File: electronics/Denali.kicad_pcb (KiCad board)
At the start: 2 copper layers, 91 parts, among them SW1 SW_SPST, SW10 SW_SPST, SW11 SW_SPST, SW12 SW_SPST, SW13 SW_SPST, SW14 SW_SPST, SW15 SW_SPST, SW16 SW_SPST, SW17 SW_SPST, SW18 SW_SPST, SW19 SW_SPST, SW2 SW_SPST, SW20 SW_SPST, SW21 SW_SPST, SW22 SW_SPST, SW23 SW_SPST, SW24 SW_SPST, SW25 SW_SPST, SW26 SW_SPST, SW27 SW_SPST, SW28 SW_SPST, SW29 SW_SPST, SW3 SW_SPST, SW30 SW_SPST, SW31 SW_SPST, SW32 SW_SPST, SW33 SW_SPST, SW34 SW_SPST, SW35 SW_SPST, SW36 SW_SPST, SW37 SW_SPST, SW38 SW_SPST, SW39 SW_SPST, SW4 SW_SPST, SW40 SW_SPST, SW41 SW_SPST, SW42 SW_SPST, SW43 SW_SPST, SW44 SW_SPST, SW45 SW_SPST, SW46 SW_SPST, SW47 SW_SPST, SW48 SW_SPST, SW49 SW_SPST, SW5 SW_SPST, SW50 SW_SPST, SW51 SW_SPST, SW52 SW_SPST, SW53 SW_SPST, SW54 SW_SPST, SW55 SW_SPST, SW56 SW_SPST, SW57 SW_SPST, SW58 SW_SPST, SW59 SW_SPST, SW6 SW_SPST, SW60 SW_SPST, SW61 SW_SPST, SW62 SW_SPST, SW63 SW_SPST, SW64 SW_SPST, SW65 SW_SPST, SW66 SW_SPST, SW67 SW_SPST, SW68 SW_SPST, SW69 SW_SPST, SW7 SW_SPST, SW70 SW_SPST, SW71 SW_SPST, SW72 SW_SPST, SW73 SW_SPST, SW74 SW_SPST, SW75 SW_SPST, SW76 SW_SPST, SW77 SW_SPST, SW78 SW_SPST, SW79 SW_SPST, SW8 SW_SPST, SW80 SW_SPST, SW81 SW_SPST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

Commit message: layout components
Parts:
- removed the SW1 at (57.0, 134.0)
- removed SW10, SW11, SW12, SW13, SW15, SW16, SW17, SW18, SW19, SW7, SW78, SW79, SW8, SW80, SW81, SW83, SW9: SW_SPST, Kailh:Kailh_socket_MX
- added SW100: SW_SPST, Kailh:Kailh_socket_MX, F.Cu at (452.0, 215.7)
- added SW101: SW_SPST, Kailh:Kailh_socket_MX, F.Cu at (471.0, 215.7)
- added SW102: SW_SPST, Kailh:Kailh_socket_MX, F.Cu at (490.0, 225.0)
- added SW104: SW_SPST, Kailh:Kailh_socket_MX, F.Cu at (442.0, 234.0)
- added SW105: SW_SPST, Kailh:Kailh_socket_MX, F.Cu at (471.0, 234.7)
- added SW87: SW_SPST, Kailh:Kailh_socket_MX, F.Cu at (413.0, 234.7)
- added SW88: SW_SPST, Kailh:Kailh_socket_MX, F.Cu at (452.0, 158.7)
- added SW89: SW_SPST, Kailh:Kailh_socket_MX, F.Cu at (471.0, 158.7)
- added SW90: SW_SPST, Kailh:Kailh_socket_MX, F.Cu at (490.0, 158.7)
- added SW91: SW_SPST, Kailh:Kailh_socket_MX, F.Cu at (433.0, 177.7)
- added SW92: SW_SPST, Kailh:Kailh_socket_MX, F.Cu at (452.0, 177.7)
- added SW93: SW_SPST, Kailh:Kailh_socket_MX, F.Cu at (471.0, 177.7)
- added SW94: SW_SPST, Kailh:Kailh_socket_MX, F.Cu at (490.0, 188.0)
- added SW95: SW_SPST, Kailh:Kailh_socket_MX, F.Cu at (433.0, 196.7)
- added SW96: SW_SPST, Kailh:Kailh_socket_MX, F.Cu at (452.0, 196.7)
- added SW97: SW_SPST, Kailh:Kailh_socket_MX, F.Cu at (471.0, 196.7)
- added SW99: SW_SPST, Kailh:Kailh_socket_MX, F.Cu at (433.0, 215.7)
- moved SW48 321.6 mm to (355.0, 158.7)
- moved SW47 306.3 mm to (336.0, 158.7)
- moved SW58 292.8 mm to (317.0, 196.7)
- moved SW51 276.2 mm to (298.0, 177.7)
- moved SW84 274.7 mm to (433.0, 158.7)
- moved SW86 264.1 mm to (394.0, 234.7)
- moved SW57 260.8 mm to (298.0, 196.7)
- moved SW82 254.6 mm to (394.0, 215.7)
- moved SW40 254.2 mm to (260.0, 158.7)
- moved SW42 247.2 mm to (202.0, 234.7)
- moved SW54 246.4 mm to (355.0, 177.7)
- moved SW53 246.0 mm to (336.0, 177.7)
- moved SW85 241.3 mm to (375.0, 234.7)
- moved SW73 240.8 mm to (355.0, 234.7)
- moved SW76 237.1 mm to (394.0, 177.7)
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- renumbered SW14 to SW1
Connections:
- SW2 pad 1: SW2 -> SW14
- SW20 pad 1: SW20 -> SW14
- SW21 pad 1: SW21 -> SW14
- SW22 pad 1: SW22 -> SW14
- SW23 pad 1: SW23 -> SW14
- SW24 pad 1: SW24 -> SW14
- SW25 pad 1: SW25 -> SW14
- SW26 pad 1: SW26 -> SW14
- SW27 pad 1: SW27 -> SW14
- SW28 pad 1: SW28 -> SW14
- SW29 pad 1: SW29 -> SW14
- SW3 pad 1: SW3 -> SW14
- SW30 pad 1: SW30 -> SW14
- SW31 pad 1: SW31 -> SW14
- SW32 pad 1: SW32 -> SW14
- SW33 pad 1: SW33 -> SW14
- SW34 pad 1: SW34 -> SW14
- SW35 pad 1: SW35 -> SW14
- SW36 pad 1: SW36 -> SW14
- SW37 pad 1: SW37 -> SW14
- SW38 pad 1: SW38 -> SW14
- SW39 pad 1: SW39 -> SW14
- SW4 pad 1: SW4 -> SW14
- SW41 pad 1: SW41 -> SW14
- SW42 pad 1: SW42 -> SW14
- SW43 pad 1: SW43 -> SW40
- SW44 pad 1: SW44 -> SW14
- SW45 pad 1: SW45 -> SW40
- SW46 pad 1: SW46 -> SW40
- SW47 pad 1: SW47 -> SW40
- SW48 pad 1: SW48 -> SW40
- SW49 pad 1: SW49 -> SW40
- SW5 pad 1: SW5 -> SW14
- SW50 pad 1: SW50 -> SW40
- SW51 pad 1: SW51 -> SW40
- SW52 pad 1: SW52 -> SW40
- SW53 pad 1: SW53 -> SW40
- SW54 pad 1: SW54 -> SW40
- SW55 pad 1: SW55 -> SW40
- SW56 pad 1: SW56 -> SW40
- SW57 pad 1: SW57 -> SW40
- SW58 pad 1: SW58 -> SW40
- SW59 pad 1: SW59 -> SW40
- SW6 pad 1: SW6 -> SW14
- SW60 pad 1: SW60 -> SW40
- SW61 pad 1: SW61 -> SW40
- SW62 pad 1: SW62 -> SW40
- SW63 pad 1: SW63 -> SW40
- SW64 pad 1: SW64 -> SW40
- SW66 pad 1: SW66 -> SW40
- SW67 pad 1: SW67 -> SW40
- SW68 pad 1: SW68 -> SW40
- SW69 pad 1: SW69 -> SW65
- SW70 pad 1: SW70 -> SW40
- SW71 pad 1: SW71 -> SW40
- SW72 pad 1: SW72 -> SW40
- SW73 pad 1: SW73 -> SW40
- SW74 pad 1: SW74 -> SW65
- SW75 pad 1: SW75 -> SW65
- SW76 pad 1: SW76 -> SW65
- SW77 pad 1: SW77 -> SW65
- SW82 pad 1: SW82 -> SW65
- SW85 pad 1: SW85 -> SW65
- SW86 pad 1: SW86 -> SW65

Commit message: add PCB edge cuts
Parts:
- U2, U3, U4, U5: moved to B.Cu
- moved U1 19.5 mm to (113.0, 151.0)
- moved U2 9.53 mm to (192.6, 143.0), turned to -90 degrees
- moved U3 5.44 mm to (308.0, 143.0), turned to 90 degrees
- moved U4 4.46 mm to (395.0, 142.0), turned to -90 degrees
- moved U5 4.46 mm to (462.0, 142.0), turned to 90 degrees
- renumbered SW23 to SW10, SW24 to SW11, SW25 to SW12, SW26 to SW13, SW27 to SW14, SW28 to SW15, SW29 to SW16, SW30 to SW17, SW31 to SW18, SW32 to SW19, SW33 to SW20, SW34 to SW21, SW35 to SW22, SW36 to SW23, SW37 to SW24, SW38 to SW25, SW39 to SW26, SW41 to SW27, SW42 to SW28, SW44 to SW29, SW40 to SW30, SW43 to SW31, SW45 to SW32, SW46 to SW33, SW47 to SW34, SW48 to SW35, SW49 to SW36, SW50 to SW37, SW51 to SW38, SW52 to SW39, SW53 to SW40, SW54 to SW41, SW55 to SW42, SW56 to SW43, SW57 to SW44, SW58 to SW45, SW59 to SW46, SW60 to SW47, SW61 to SW48, SW62 to SW49, SW63 to SW50, SW64 to SW51, SW66 to SW52, SW67 to SW53, SW68 to SW54, SW70 to SW55, SW71 to SW56, SW72 to SW57, SW73 to SW58, SW65 to SW59, SW69 to SW60, SW74 to SW61, SW75 to SW62, SW76 to SW63, SW77 to SW64, SW82 to SW65, SW85 to SW66, SW86 to SW67, SW87 to SW68, SW84 to SW69, SW20 to SW7, SW88 to SW70, SW89 to SW71, SW90 to SW72, SW91 to SW73, SW92 to SW74, SW93 to SW75, SW94 to SW76, SW95 to SW77, SW96 to SW78, SW97 to SW79, SW21 to SW8, SW99 to SW80, SW100 to SW81, SW101 to SW82, SW102 to SW83, SW104 to SW84, SW105 to SW85, SW22 to SW9
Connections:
- SW1 pad 1: SW14 -> SW1
- SW10 pad 1: SW14 -> SW10
- SW11 pad 1: SW14 -> SW11
- SW12 pad 1: SW14 -> SW12
- SW13 pad 1: SW14 -> SW13
- SW15 pad 1: SW14 -> SW15
- SW16 pad 1: SW14 -> SW16
- SW17 pad 1: SW14 -> SW17
- SW18 pad 1: SW14 -> SW18
- SW19 pad 1: SW14 -> SW19
- SW2 pad 1: SW14 -> SW2
- SW20 pad 1: SW14 -> SW20
- SW21 pad 1: SW14 -> SW21
- SW22 pad 1: SW14 -> SW22
- SW23 pad 1: SW14 -> SW23
- SW24 pad 1: SW14 -> SW24
- SW25 pad 1: SW14 -> SW25
- SW26 pad 1: SW14 -> SW26
- SW27 pad 1: SW14 -> SW27
- SW28 pad 1: SW14 -> SW28
- SW29 pad 1: SW14 -> SW29
- SW3 pad 1: SW14 -> SW3
- SW30 pad 1: SW40 -> SW30
- SW31 pad 1: SW40 -> SW31
- SW32 pad 1: SW40 -> SW32
- SW33 pad 1: SW40 -> SW33
- SW34 pad 1: SW40 -> SW34
- SW35 pad 1: SW40 -> SW35
- SW36 pad 1: SW40 -> SW36
- SW37 pad 1: SW40 -> SW37
- SW38 pad 1: SW40 -> SW38
- SW39 pad 1: SW40 -> SW39
- SW4 pad 1: SW14 -> SW4
- SW41 pad 1: SW40 -> SW41
- SW42 pad 1: SW40 -> SW42
- SW43 pad 1: SW40 -> SW43
- SW44 pad 1: SW40 -> SW44
- SW45 pad 1: SW40 -> SW45
- SW46 pad 1: SW40 -> SW46
- SW47 pad 1: SW40 -> SW47
- SW48 pad 1: SW40 -> SW48
- SW49 pad 1: SW40 -> SW49
- SW5 pad 1: SW14 -> SW5
- SW50 pad 1: SW40 -> SW50
- SW51 pad 1: SW40 -> SW51
- SW52 pad 1: SW40 -> SW52
- SW53 pad 1: SW40 -> SW53
- SW54 pad 1: SW40 -> SW54
- SW55 pad 1: SW40 -> SW55
- SW56 pad 1: SW40 -> SW56
- SW57 pad 1: SW40 -> SW57
- SW58 pad 1: SW40 -> SW58
- SW59 pad 1: SW65 -> SW59
- SW6 pad 1: SW14 -> SW6
- SW60 pad 1: SW65 -> SW60
- SW61 pad 1: SW65 -> SW61
- SW62 pad 1: SW65 -> SW62
- SW63 pad 1: SW65 -> SW63
- SW64 pad 1: SW65 -> SW64
- SW66 pad 1: SW65 -> SW66
- SW67 pad 1: SW65 -> SW67
- SW68 pad 1: SW65 -> SW68
- SW69 pad 1: SW84 -> SW69
- SW7 pad 1: SW14 -> SW7
- SW70 pad 1: SW84 -> SW70
- SW71 pad 1: SW84 -> SW71
- SW72 pad 1: SW84 -> SW72
- SW73 pad 1: SW84 -> SW73
- SW74 pad 1: SW84 -> SW74
- SW75 pad 1: SW84 -> SW75
- SW76 pad 1: SW84 -> SW76
- SW77 pad 1: SW84 -> SW77
- SW78 pad 1: SW84 -> SW78
- SW79 pad 1: SW84 -> SW79
- SW8 pad 1: SW14 -> SW8
- SW80 pad 1: SW84 -> SW80
- SW81 pad 1: SW84 -> SW81
- SW82 pad 1: SW84 -> SW82
- SW83 pad 1: SW84 -> SW83
- SW85 pad 1: SW84 -> SW85
- SW9 pad 1: SW14 -> SW9
- U1 pad 18: unconnected-(U1-Pad18) -> +3V3
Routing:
- added copper zone on F.Cu, net +3V3
- added copper zone on B.Cu, net GND
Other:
- board outline added: 410 x 115 mm

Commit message: change IO expanders and add 3D models
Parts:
- U1: value kb2040 -> ProMicro
- U2, U3: value PCA9506DGG -> PCA9675PW; footprint PCA9506:PCA9506DGG -> PCA9675PW:SOP65P640X110-24N
- U4, U5: value MAX7314AEG+ -> PCA9675PW; footprint MAX7314AEG:MAX7314AEG&plus_ -> PCA9675PW:SOP65P640X110-24N
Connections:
- U2 pad 1: SDA0 -> unconnected-(U2-Pad1)
- U2 pad 2: SCL0 -> unconnected-(U2-Pad2)
- U2 pad 22: unconnected-(U2-Pad22) -> SCL0
- U2 pad 23: unconnected-(U2-Pad23) -> SDA0
- U3 pad 1: SDA0 -> unconnected-(U3-Pad1)
- U3 pad 2: SCL0 -> unconnected-(U3-Pad2)
- U3 pad 22: unconnected-(U3-Pad22) -> SCL0
- U3 pad 23: unconnected-(U3-Pad23) -> SDA0
- U4 pad 22: SCL1 -> SDA1
- U4 pad 23: SDA1 -> SCL1
- U5 pad 22: SCL1 -> SDA1
- U5 pad 23: SDA1 -> SCL1

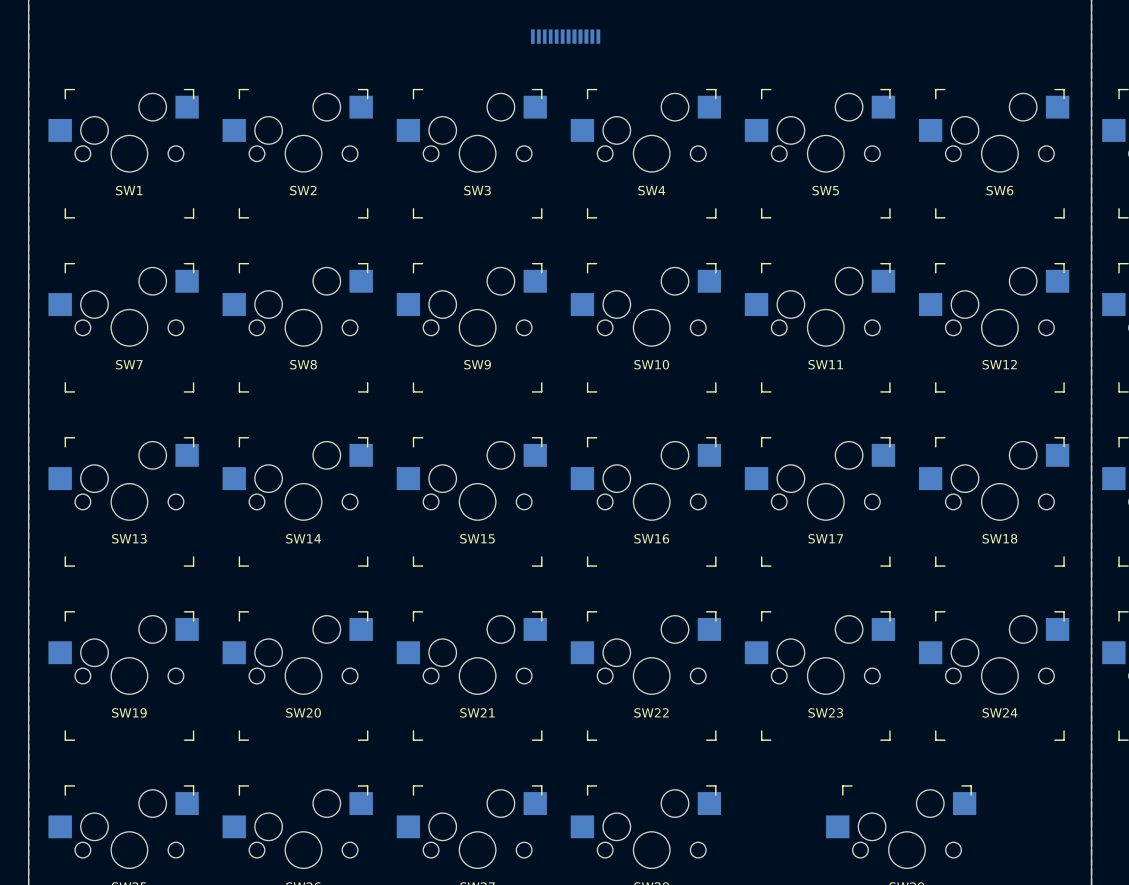
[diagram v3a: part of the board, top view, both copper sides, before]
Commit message: begin mini-matrix routing
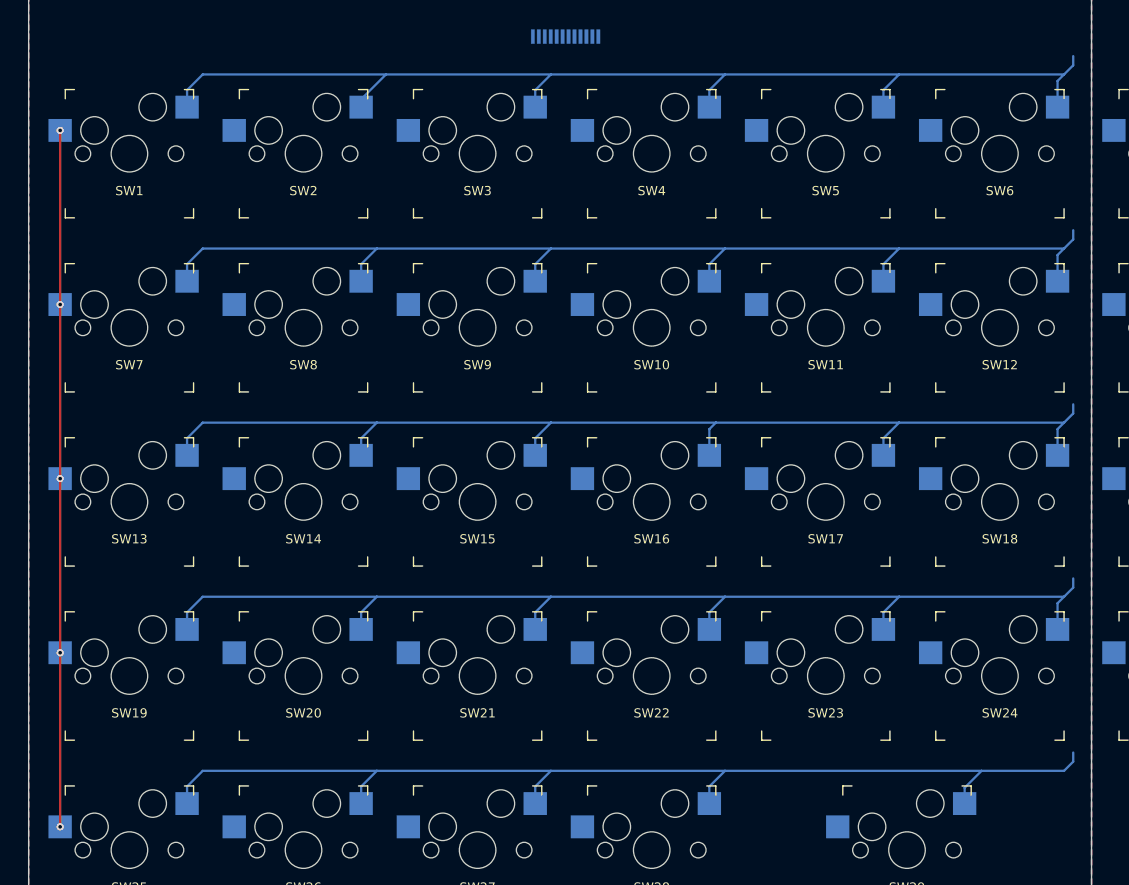
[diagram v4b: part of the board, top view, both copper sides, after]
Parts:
- U1: value ProMicro -> kb2040
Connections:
- SW1 pad 1: SW1 -> ROW00
- SW1 pad 2: GND -> COL00
- SW10 pad 1: SW10 -> ROW01
- SW10 pad 2: GND -> COL03
- SW11 pad 1: SW11 -> ROW01
- SW11 pad 2: GND -> COL04
- SW12 pad 1: SW12 -> ROW01
- SW12 pad 2: GND -> COL05
- SW13 pad 1: SW13 -> ROW02
- SW13 pad 2: GND -> COL00
- SW14 pad 1: SW14 -> ROW02
- SW14 pad 2: GND -> COL01
- SW15 pad 1: SW15 -> ROW02
- SW15 pad 2: GND -> COL02
- SW16 pad 1: SW16 -> ROW02
- SW16 pad 2: GND -> COL03
- SW17 pad 1: SW17 -> ROW02
- SW17 pad 2: GND -> COL04
- SW18 pad 1: SW18 -> ROW02
- SW18 pad 2: GND -> COL05
- SW19 pad 1: SW19 -> ROW03
- SW19 pad 2: GND -> COL00
- SW2 pad 1: SW2 -> ROW00
- SW2 pad 2: GND -> COL01
- SW20 pad 1: SW20 -> ROW03
- SW20 pad 2: GND -> COL01
- SW21 pad 1: SW21 -> ROW03
- SW21 pad 2: GND -> COL02
- SW22 pad 1: SW22 -> ROW03
- SW22 pad 2: GND -> COL03
- SW23 pad 1: SW23 -> ROW03
- SW23 pad 2: GND -> COL04
- SW24 pad 1: SW24 -> ROW03
- SW24 pad 2: GND -> COL05
- SW25 pad 1: SW25 -> ROW04
- SW25 pad 2: GND -> COL00
- SW26 pad 1: SW26 -> ROW04
- SW26 pad 2: GND -> COL01
- SW27 pad 1: SW27 -> ROW04
- SW27 pad 2: GND -> COL02
- SW28 pad 1: SW28 -> ROW04
- SW28 pad 2: GND -> COL03
- SW29 pad 1: SW29 -> ROW04
- SW29 pad 2: GND -> COL05
- SW3 pad 1: SW3 -> ROW00
- SW3 pad 2: GND -> COL02
- SW4 pad 1: SW4 -> ROW00
- SW4 pad 2: GND -> COL03
- SW5 pad 1: SW5 -> ROW00
- SW5 pad 2: GND -> COL04
- SW6 pad 1: SW6 -> ROW00
- SW6 pad 2: GND -> COL05
- SW7 pad 1: SW7 -> ROW01
- SW7 pad 2: GND -> COL00
- SW8 pad 1: SW8 -> ROW01
- SW8 pad 2: GND -> COL01
- SW9 pad 1: SW9 -> ROW01
- SW9 pad 2: GND -> COL02
- U2 pad 1: unconnected-(U2-Pad1) -> ~{INT}
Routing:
- net ROW00: track 0.00 -> 122.1 mm
- net ROW01: track 0.00 -> 121.7 mm
- net ROW03: track 0.00 -> 121.7 mm
- net ROW02: track 0.00 -> 121.3 mm
- net ROW04: track 0.00 -> 117.9 mm
- net COL00: track 0.00 -> 76.5 mm, vias 0 -> 5
